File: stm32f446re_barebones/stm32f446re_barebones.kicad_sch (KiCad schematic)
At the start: 23 parts, among them SW1 SW_SPDT, SW2 SW_Push, U1 STM32F446RETx, Y1 16mhz

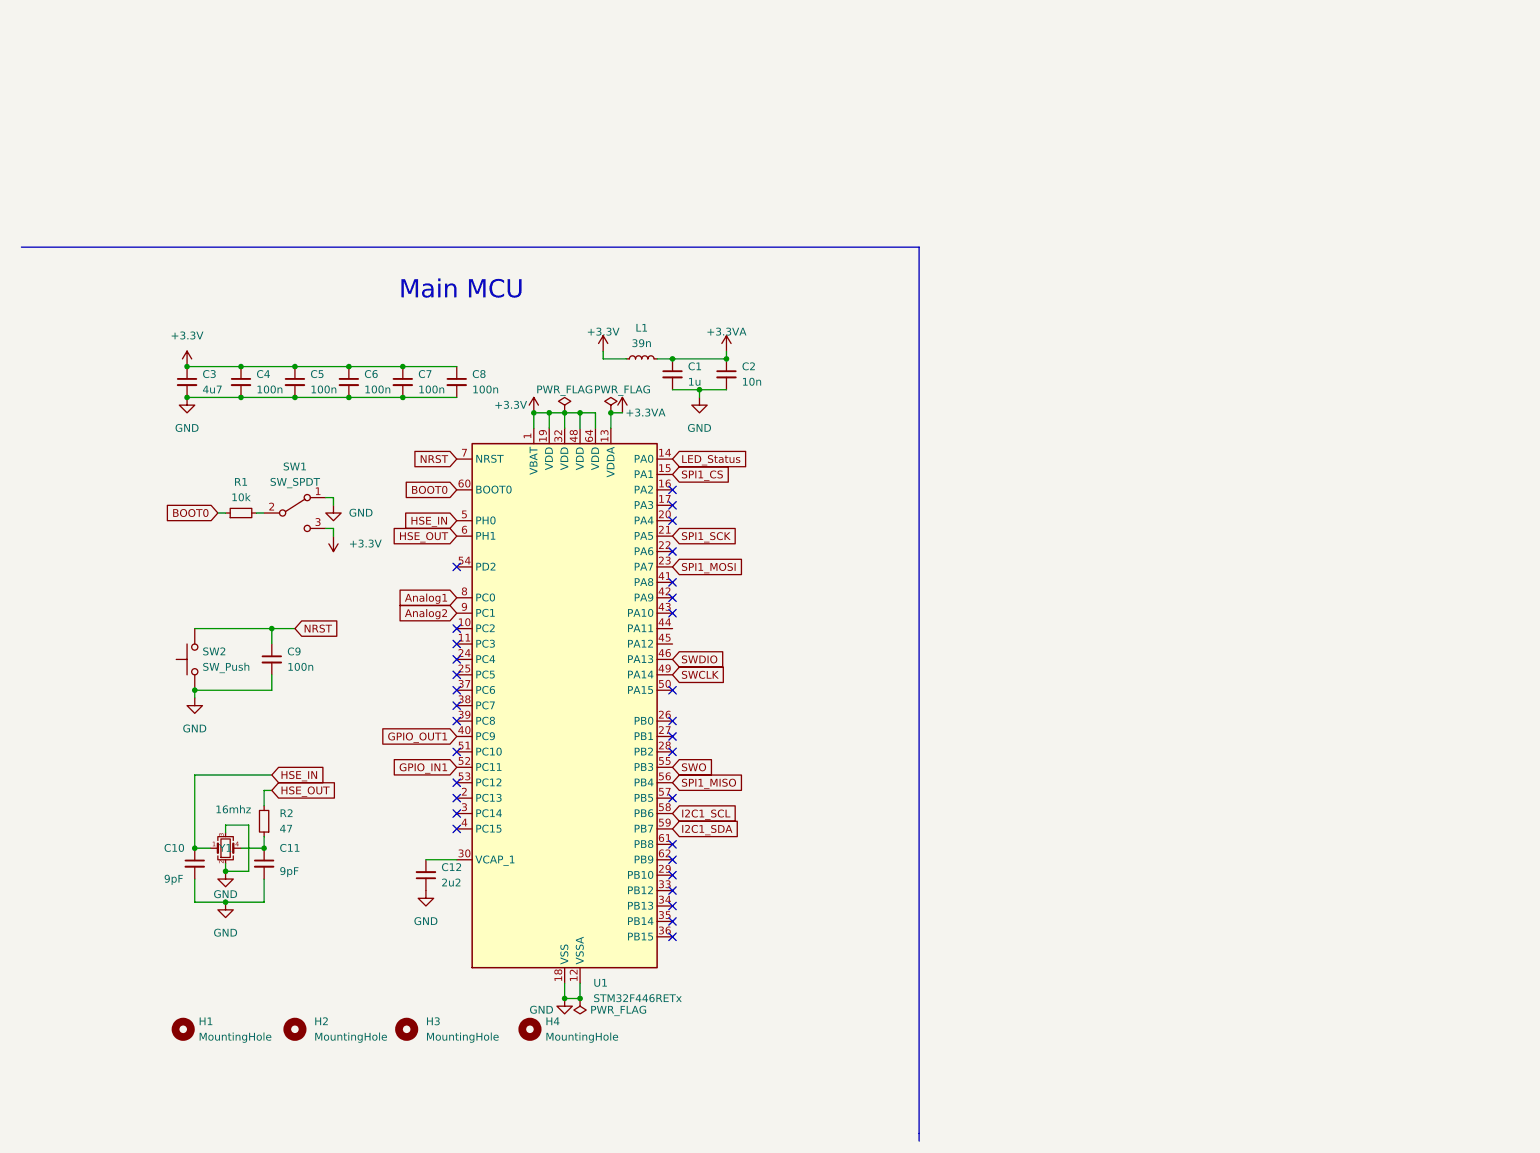
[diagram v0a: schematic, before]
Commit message: finished the schematics, added footprints, and started with the pcb
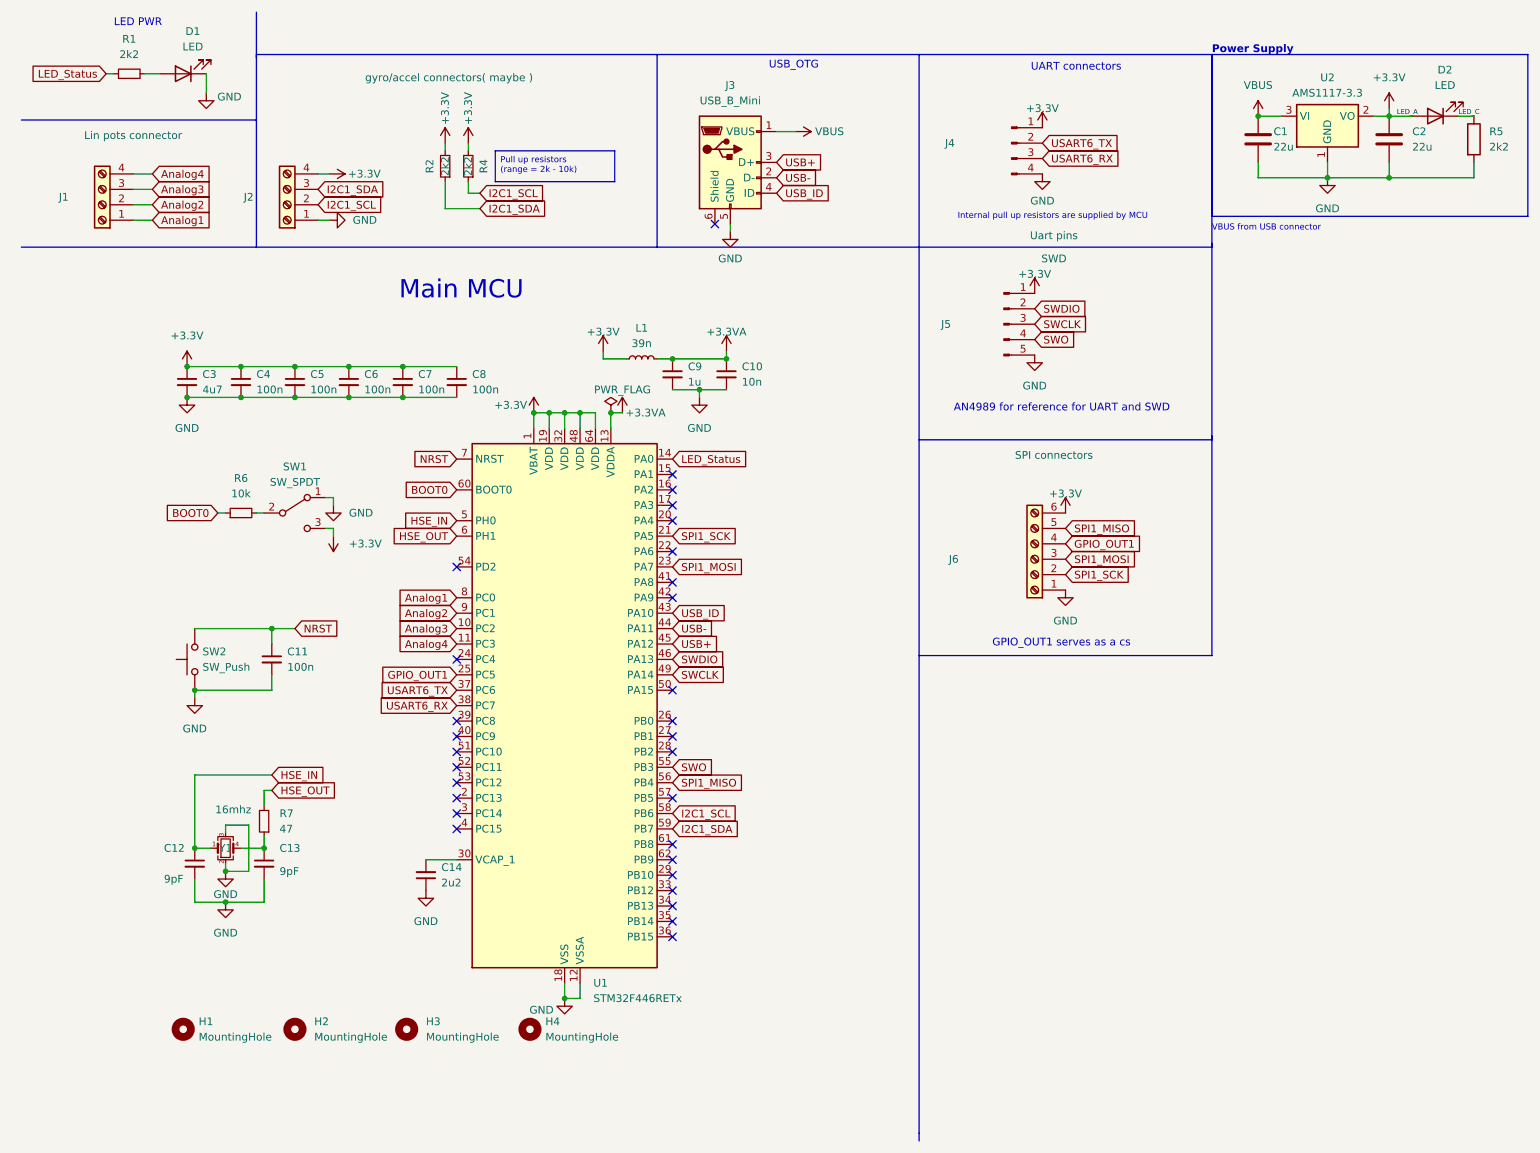
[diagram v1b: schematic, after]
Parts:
- added C1: 22u, Capacitor_SMD:C_0603_1608Metric, symbol Device:C
- added C2: 22u, Capacitor_SMD:C_0805_2012Metric, symbol Device:C
- added D1, D2: LED, LED_SMD:LED_1210_3225Metric, symbol Device:LED
- added J1: Lin pots connector, TerminalBlock_Phoenix:TerminalBlock_Phoenix_MKDS-1,5-4_1x04_P5.00mm_Horizontal, symbol Connector:Screw_Terminal_01x04
- added J2: gyro/accel connectors( maybe ), TerminalBlock_Phoenix:TerminalBlock_Phoenix_MKDS-1,5-4_1x04_P5.00mm_Horizontal, symbol Connector:Screw_Terminal_01x04
- added J3: USB_B_Mini, Connector_USB:USB_Mini-B_AdamTech_MUSB-B5-S-VT-TSMT-1_SMD_Vertical, symbol Connector:USB_B_Micro
- added J4: Uart pins, Connector_PinHeader_2.54mm:PinHeader_1x04_P2.54mm_Horizontal, symbol Connector:Conn_01x04_Pin
- added J5: SWD, Connector_PinHeader_2.54mm:PinHeader_1x05_P2.54mm_Horizontal, symbol Connector:Conn_01x05_Pin
- added J6: SPI connectors, TerminalBlock_Phoenix:TerminalBlock_Phoenix_MKDS-1,5-6-5.08_1x06_P5.08mm_Horizontal, symbol Connector:Screw_Terminal_01x06
- added R1, R2, R4: 2k2, Resistor_SMD:R_0805_2012Metric, symbol Device:R_Small
- added R5: 2k2, Resistor_SMD:R_0402_1005Metric_Pad0.72x0.64mm_HandSolder, symbol Device:R
- added U2: AMS1117-3.3, Package_TO_SOT_SMD:SOT-223-3_TabPin2, symbol Regulator_Linear:AMS1117-3.3
- C10: renamed from C2; footprint (none) -> Capacitor_SMD:C_0805_2012Metric
- C11: renamed from C9; footprint (none) -> Capacitor_SMD:C_0805_2012Metric
- C12: renamed from C10; footprint (none) -> Capacitor_SMD:C_0805_2012Metric
- C13: renamed from C11; footprint (none) -> Capacitor_SMD:C_0805_2012Metric
- C14: renamed from C12; footprint (none) -> Capacitor_SMD:C_0805_2012Metric
- C3, C4, C5, C6, C7, C8: footprint (none) -> Capacitor_SMD:C_0805_2012Metric
- C9: renamed from C1; footprint (none) -> Capacitor_SMD:C_0805_2012Metric
- H1, H2, H3, H4: footprint (none) -> MountingHole:MountingHole_2.2mm_M2_DIN965_Pad
- L1: footprint (none) -> Inductor_SMD:L_0805_2012Metric
- R6: renamed from R1; footprint (none) -> Resistor_SMD:R_0805_2012Metric
- R7: renamed from R2; footprint (none) -> Resistor_SMD:R_0805_2012Metric
- SW1: footprint (none) -> Button_Switch_SMD:SW_SPDT_PCM12
- SW2: footprint (none) -> Button_Switch_SMD:SW_SPST_B3U-1000P-B
- Y1: footprint (none) -> Oscillator:Oscillator_SMD_Kyocera_KC2520Z-4Pin_2.5x2.0mm
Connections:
- net +3.3V: now also C2.1, D2.2 (A), J2.4 (Pin_4), J4.1 (Pin_1), J5.1 (Pin_1), J6.6 (Pin_6), R2.2, R4.2, U2.2 (VO)
- net Analog1: now also J1.1 (Pin_1)
- net Analog2: now also J1.2 (Pin_2)
- net GND: now also C1.2, C2.2, D1.1 (K), J2.1 (Pin_1), J3.5 (GND), J4.4 (Pin_4), J5.5 (Pin_5), J6.1 (Pin_1), R5.2, U2.1 (GND)
- net GPIO_OUT1: now also U1.25 (PC5), J6.4 (Pin_4); no longer U1.40 (PC9)
- net I2C1_SCL: now also J2.2 (Pin_2), R4.1
- net I2C1_SDA: now also J2.3 (Pin_3), R2.1
- net LED_Status: now also R1.1
- net SPI1_MISO: now also J6.5 (Pin_5)
- net SPI1_MOSI: now also J6.3 (Pin_3)
- net SPI1_SCK: now also J6.2 (Pin_2)
- net SWCLK: now also J5.3 (Pin_3)
- net SWDIO: now also J5.2 (Pin_2)
- net SWO: now also J5.4 (Pin_4)
- net Analog3: now reaches U1.10 (PC2)
- net Analog3: now also J1.3 (Pin_3)
- net Analog4: now reaches U1.11 (PC3)
- net Analog4: now also J1.4 (Pin_4)
- net USART6_TX: now reaches U1.37 (PC6)
- net USART6_TX: now also J4.2 (Pin_2)
- net USART6_RX: now reaches U1.38 (PC7)
- net USART6_RX: now also J4.3 (Pin_3)
- net USB_ID: now reaches U1.43 (PA10)
- net USB_ID: now also J3.4 (ID)
- net USB-: now reaches U1.44 (PA11)
- net USB-: now also J3.2 (D-)
- net USB+: now reaches U1.45 (PA12)
- net USB+: now also J3.3 (D+)
- net GPIO_IN1: no longer names the net of U1.52 (PC11)
- net SPI1_CS: no longer names the net of U1.15 (PA1)
- new net: D1.2 (A), R1.2
- new net LED_C: D2.1 (K), R5.1
- new net VBUS: C1.1, J3.1 (VBUS), U2.3 (VI)
- no-connect marks 32 -> 30
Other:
- note added: "AN4989 for reference for UART and SWD"
- note added: "GPIO_OUT1 serves as a cs"
- note added: "Internal pull up resistors are supplied by MCU"
- note added: "LED PWR"
- note added: "Power Supply"
- note added: "UART connectors"
- note added: "USB_OTG"
- note added: "VBUS from USB connector"

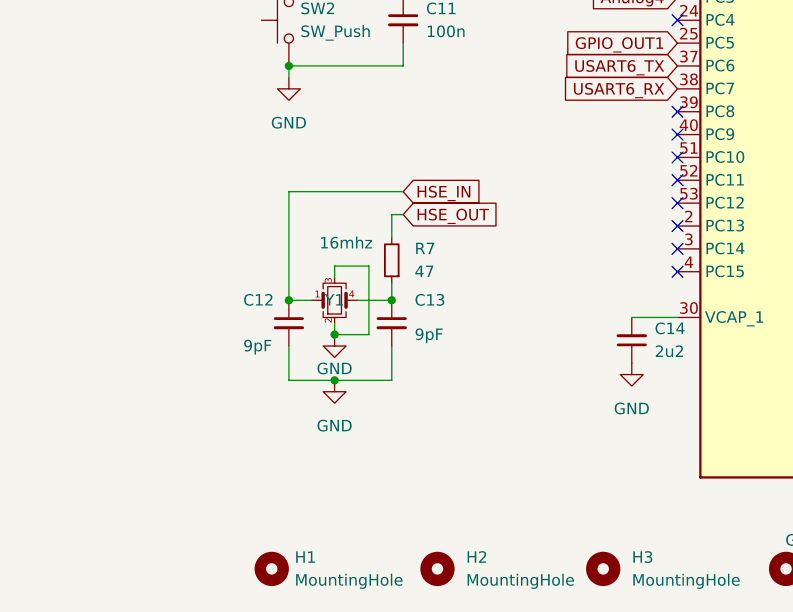
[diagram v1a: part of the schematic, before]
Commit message: PCB routing. Need to do USB differential pair. Also usb maybe backwards
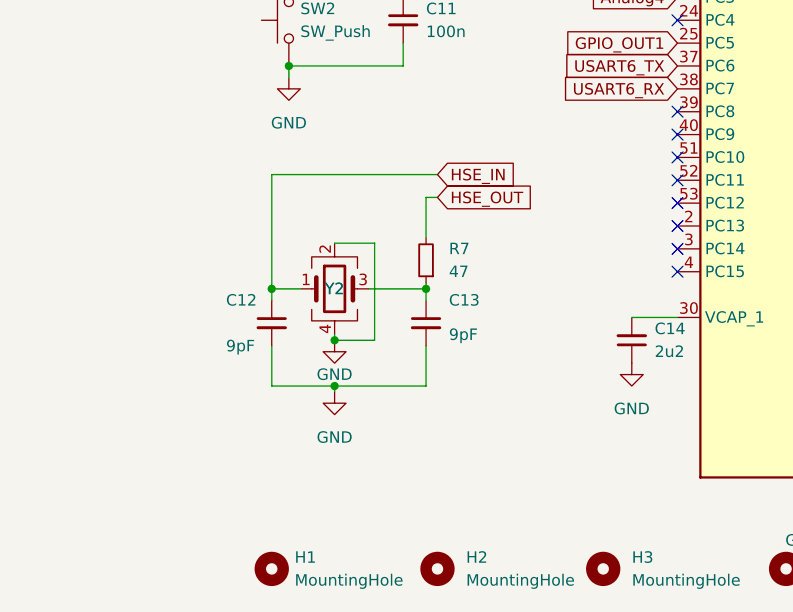
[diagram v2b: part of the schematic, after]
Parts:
- removed Y1: 16mhz, Oscillator:Oscillator_SMD_Kyocera_KC2520Z-4Pin_2.5x2.0mm, symbol Device:Crystal_GND23_Small
- added Y2: Y2, Crystal:Crystal_SMD_3225-4Pin_3.2x2.5mm, symbol Device:Crystal_GND24
- C10, C11, C12, C13, C14, C2, C3, C4, C5, C6, C7, C8, C9: footprint Capacitor_SMD:C_0805_2012Metric -> Capacitor_SMD:C_0603_1608Metric
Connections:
- net GND: now also Y2.2, Y2.4
- net HSE_IN: now also Y2.1
- net at C13.1, R7.1: now also Y2.3
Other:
- moved on the sheet: C12, C13, R7

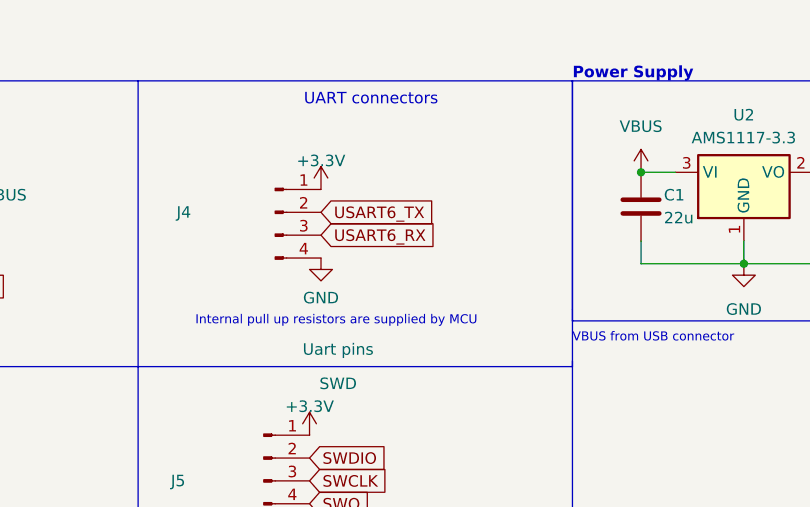
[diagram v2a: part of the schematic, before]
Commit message: Removed resistor at the ina- termina
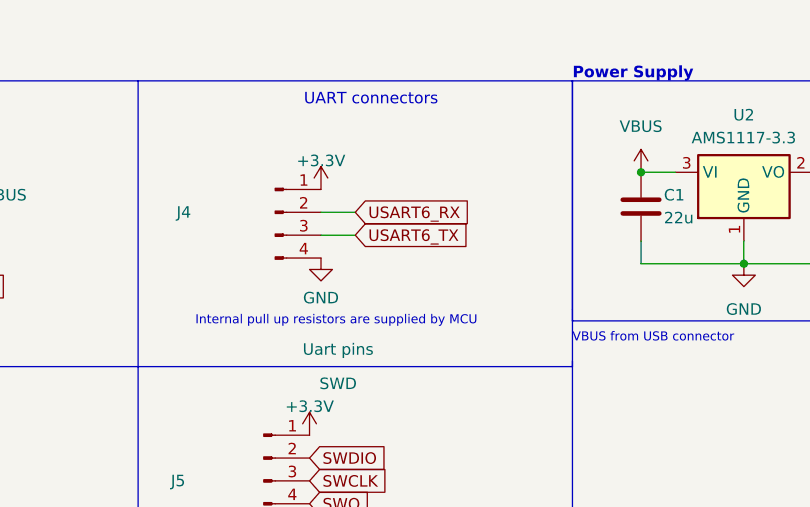
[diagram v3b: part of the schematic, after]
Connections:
- net USART6_RX: now also J4.2 (Pin_2); no longer J4.3 (Pin_3)
- net USART6_TX: now also J4.3 (Pin_3); no longer J4.2 (Pin_2)
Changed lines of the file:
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@@
+    (stroke (width 0) (type default))
+  )
+  (wire (pts (xy 180.34 33.655) (xy 184.15 33.655))
     (stroke (width 0) (type default))
   )
@@
   )
   (polyline (pts (xy 208.28 81.915) (xy 208.28 118.11))
+    (stroke (width 0) (type default))
+  )
+  (wire (pts (xy 180.34 36.195) (xy 184.15 36.195))
     (stroke (width 0) (type default))
   )
@@
     )
   )
-  (global_label "USART6_RX" (shape input) (at 180.34 36.195 0) (fields_autoplaced)
-    (effects (font (size 1.27 1.27)) (justify left))
-    (property "Intersheetrefs" "${INTERSHEET_REFS}" (at 193.848 36.195 0)
+  (global_label "USART6_RX" (shape input) (at 184.15 33.655 0) (fields_autoplaced)
+    (effects (font (size 1.27 1.27)) (justify left))
+    (property "Intersheetrefs" "${INTERSHEET_REFS}" (at 197.658 33.655 0)
       (effects (font (size 1.27 1.27)) (justify left) hide)
     )
@@
     )
   )
-  (global_label "USART6_TX" (shape input) (at 180.34 33.655 0) (fields_autoplaced)
-    (effects (font (size 1.27 1.27)) (justify left))
-    (property "Intersheetrefs" "${INTERSHEET_REFS}" (at 193.5456 33.655 0)
-      (effects (font (size 1.27 1.27)) (justify left) hide)
-    )
+  (global_label "USART6_TX" (shape input) (at 184.15 36.195 0) (fields_autoplaced)
+    (effects (font (size 1.27 1.27)) (justify left))
+    (property "Intersheetrefs" "${INTERSHEET_REFS}" (at 197.3556 36.195 0)
+      (effects (font (size 1.27 1.27)) (justify left) hide)
+    )

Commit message: tweaked some stuff for the daq and added a files
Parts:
- J3: footprint Connector_USB:USB_Mini-B_AdamTech_MUSB-B5-S-VT-TSMT-1_SMD_Vertical -> Connector_USB:USB_Mini-B_Lumberg_2486_01_Horizontal
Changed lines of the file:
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@@
       (effects (font (size 1.27 1.27)))
     )
-    (property "Footprint" "Connector_USB:USB_Mini-B_AdamTech_MUSB-B5-S-VT-TSMT-1_SMD_Vertical" (at 132.715 38.1 0)
+    (property "Footprint" "Connector_USB:USB_Mini-B_Lumberg_2486_01_Horizontal" (at 132.715 38.1 0)
       (effects (font (size 1.27 1.27)) hide)
     )
